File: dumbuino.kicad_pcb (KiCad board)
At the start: 4 copper layers, 68.6 x 53.3 mm, 44 parts, among them J1 USB_C_Receptacle_USB2.0, J2 Conn_01x02_Male, J3 Conn_01x02_Male, P1 Power, P2 Analog, P3 Digital, P4 Digital, P5 CONN_01X01, P6 CONN_01X01, P7 CONN_01X01, P8 CONN_01X01, Q1 Q_NMOS_GDS, Q2 Q_NMOS_GDS, U1 FT232RL, U2 ATmega328PB-AU, Y1 16M

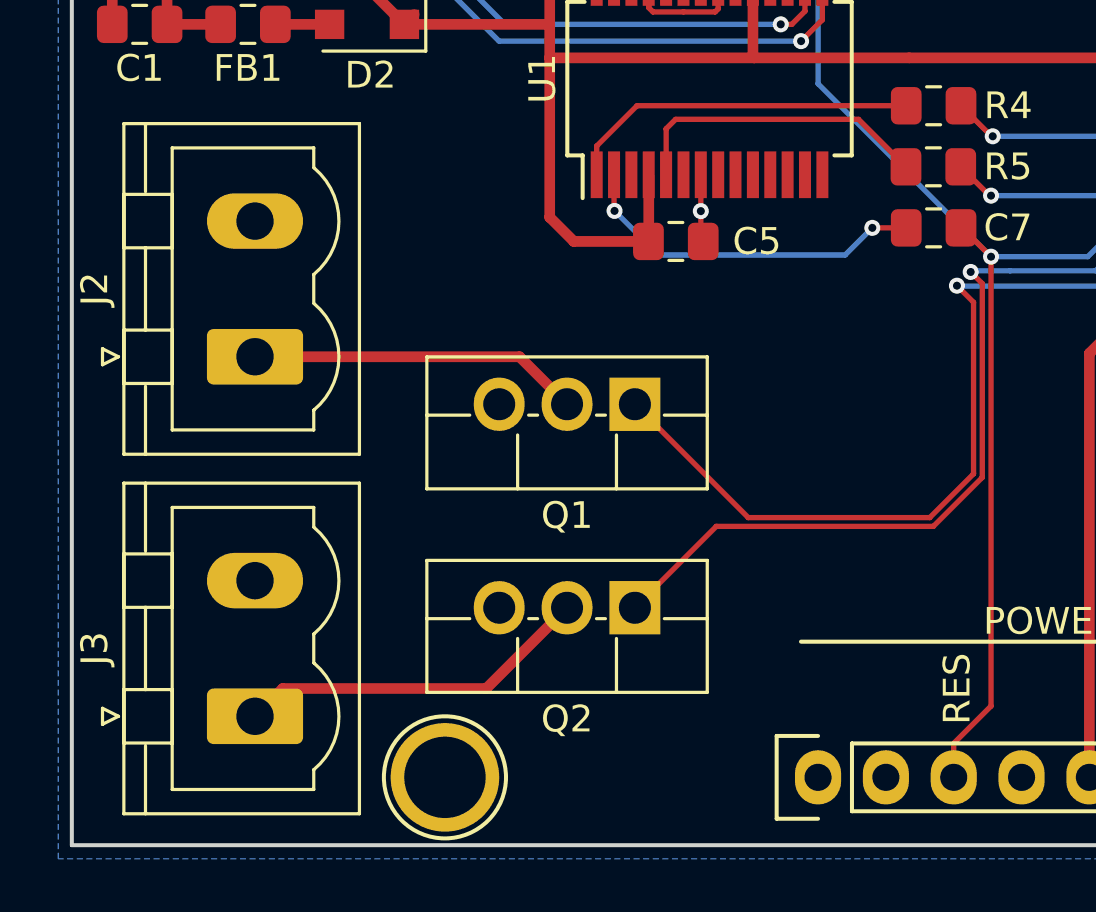
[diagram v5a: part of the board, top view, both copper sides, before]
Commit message: Update track width
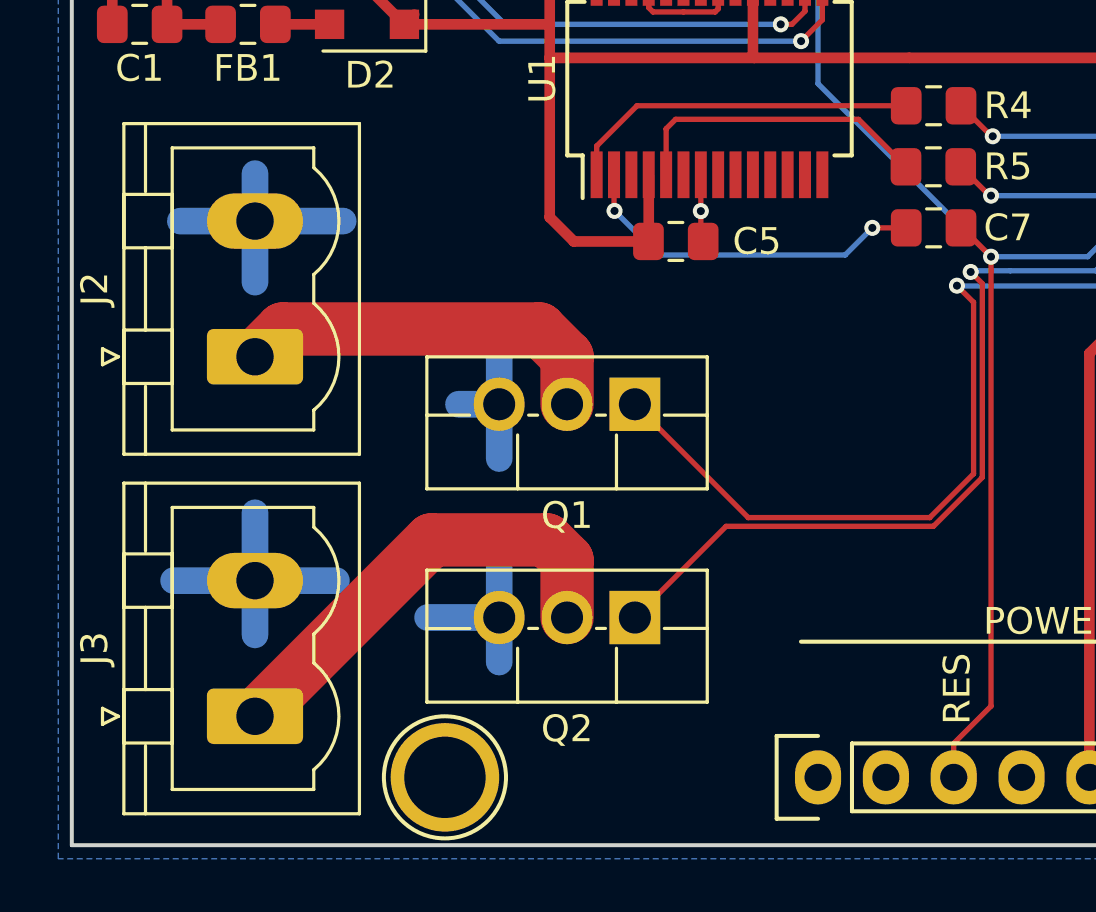
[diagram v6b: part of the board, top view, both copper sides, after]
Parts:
- moved Q2 0.37 mm to (132.1, 117.8)
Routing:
- net GND: track 40.3 -> 73.5 mm
- net Net-(J3-Pad1): track 13.4 -> 16.9 mm
- net Net-(J2-Pad1): track 12.4 -> 14.3 mm

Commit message: Updated values
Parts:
- removed PWR: PWR, LED_SMD:LED_0805_2012Metric_Pad1.15x1.40mm_HandSolder
- added D1: PWR, LED_SMD:LED_0805_2012Metric_Pad1.15x1.40mm_HandSolder, F.Cu at (134.9, 88.8)
- C1: value 0.01 -> 0.01u
- C3, C4, C5, C6, C7, C8: value 0.1 -> 0.1u
- renumbered RX to D3, TX to D4, RES to D5, 13 to D6, Reset to SW1
